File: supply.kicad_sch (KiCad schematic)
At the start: 71 parts, among them U1 AP7330-W5-7, U2 AP7330-W5-7, U3 AP7330-W5-7, U4 AP62301WU-7, U5 AP62301WU-7, U6 AP62301WU-7, U8 NCV51200MNTXG

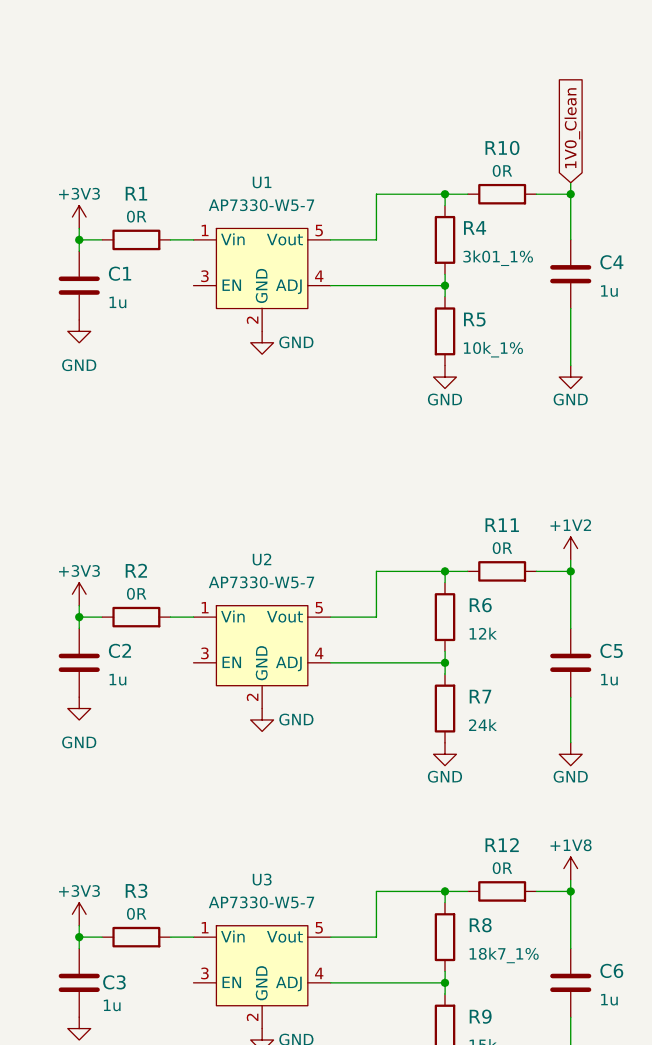
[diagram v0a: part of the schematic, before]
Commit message: Connected soft MIPI CSI to FPGA
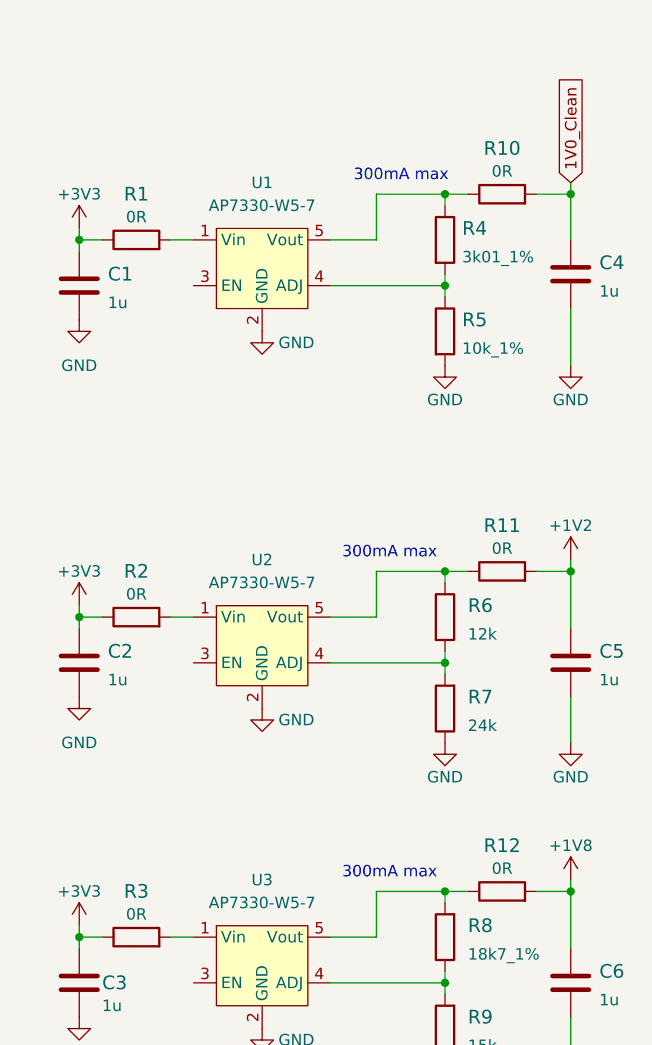
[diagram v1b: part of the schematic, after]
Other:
- note added: "300mA max"
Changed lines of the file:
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@@
     (stroke (width 0) (type default) (color 0 0 0 0))
+  )
+  (text "300mA max" (at 231.14 80.01 0)
+    (effects (font (size 1.27 1.27)) (justify left bottom))
   )
   (text "Sense line" (at 106.68 156.21 0)
@@
   )
   (text "Nominal currents are lower than rated" (at 115.57 138.43 0)
+    (effects (font (size 1.27 1.27)) (justify left bottom))
+  )
+  (text "300mA max" (at 231.14 115.57 0)
     (effects (font (size 1.27 1.27)) (justify left bottom))
   )
@@
     (effects (font (size 1.27 1.27)) (justify left bottom))
   )
+  (text "300mA max" (at 232.41 38.1 0)
+    (effects (font (size 1.27 1.27)) (justify left bottom))
+  )

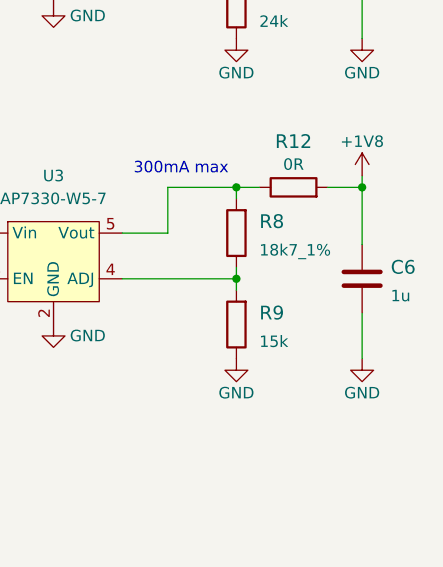
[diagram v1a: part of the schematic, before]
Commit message: Connected FPGA to power supply and added power filtering
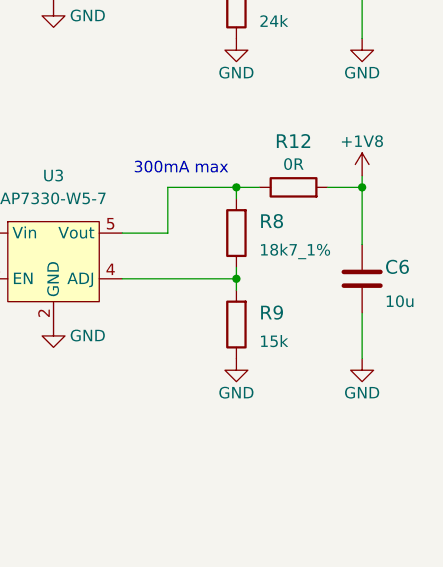
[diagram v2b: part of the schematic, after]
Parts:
- removed C6: C_1u_0603, antmicro-footprints:0603-cap, symbol antmicroCapacitors0603:C_1u_0603
- added C6: C_10u_0603, antmicro-footprints:0603-cap, symbol antmicroCapacitors0603:C_10u_0603
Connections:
- net +1V8: now also C6.1
- net GND: now also C6.2
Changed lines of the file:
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@@
-    (pin "2")
-  )
-  (symbol (lib_id "antmicroCapacitors0603:C_1u_0603") (at 256.54 127 0) (unit 1)
-    (in_bom yes) (on_board yes) (fields_autoplaced)
-    (property "Reference" "C6" (id 0) (at 259.715 125.73 0)
-      (effects (font (size 1.524 1.524)) (justify left))
-    )
-    (property "Value" "C_1u_0603" (id 1) (at 256.54 130.81 0)
-      (effects (font (size 1.524 1.524)) hide)
-    )
-    (property "Footprint" "antmicro-footprints:0603-cap" (id 2) (at 261.62 121.92 0)
-      (effects (font (size 1.524 1.524)) (justify left) hide)
-    )
-    (property "Datasheet" "" (id 3) (at 256.54 127 0)
-      (effects (font (size 1.27 1.27)) hide)
-    )
-    (property "Manufacturer" "WALSIN" (id 4) (at 261.62 116.84 0)
-      (effects (font (size 1.524 1.524)) (justify left) hide)
-    )
-    (property "MPN" "0603YD105KAT2A" (id 5) (at 261.62 119.38 0)
-      (effects (font (size 1.524 1.524)) (justify left) hide)
-    )
-    (property "Val" "1u" (id 6) (at 259.715 128.9049 0)
-      (effects (font (size 1.27 1.27)) (justify left))
-    )
-    (pin "1")
     (pin "2")
   )
@@
     (pin "1")
   )
+  (symbol (lib_id "antmicroCapacitors0603:C_10u_0603") (at 256.54 127 0) (unit 1)
+    (in_bom yes) (on_board yes)
+    (property "Reference" "C6" (id 0) (at 259.08 125.73 0)
+      (effects (font (size 1.524 1.524)) (justify left))
+    )
+    (property "Value" "C_10u_0603" (id 1) (at 256.54 130.81 0)
+      (effects (font (size 1.524 1.524)) hide)
+    )
+    (property "Footprint" "antmicro-footprints:0603-cap" (id 2) (at 261.62 121.92 0)
+      (effects (font (size 1.524 1.524)) (justify left) hide)
+    )
+    (property "Datasheet" "" (id 3) (at 256.54 127 0)
+      (effects (font (size 1.27 1.27)) hide)
+    )
+    (property "Manufacturer" "Murata" (id 4) (at 261.62 116.84 0)
+      (effects (font (size 1.524 1.524)) (justify left) hide)
+    )
+    (property "MPN" "GRM188R61A106KE69D" (id 5) (at 261.62 119.38 0)
+      (effects (font (size 1.524 1.524)) (justify left) hide)
+    )
+    (property "Val" "10u" (id 6) (at 259.08 129.54 0)
+      (effects (font (size 1.27 1.27)) (justify left))
+    )
+    (pin "1")
+    (pin "2")
+  )
   (symbol (lib_id "antmicroResistorsmisc:R_0R_0805") (at 160.02 24.765 0) (unit 1)

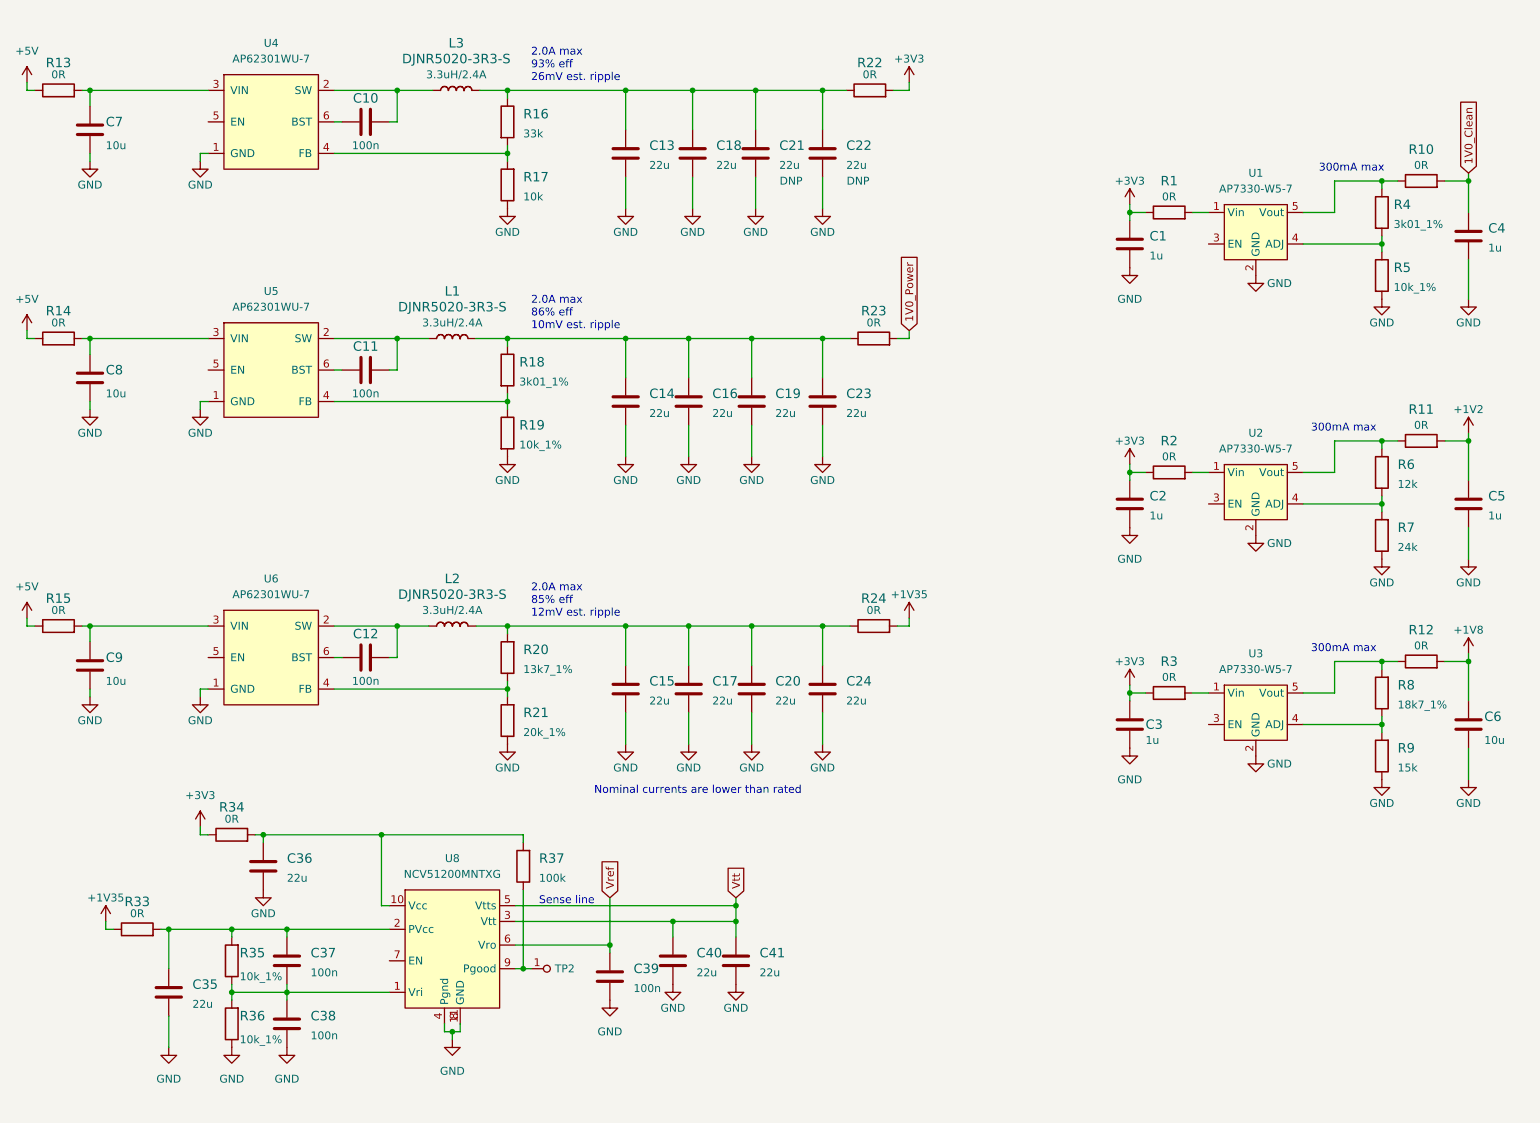
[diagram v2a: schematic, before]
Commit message: Connected EN pins on PSU schematic
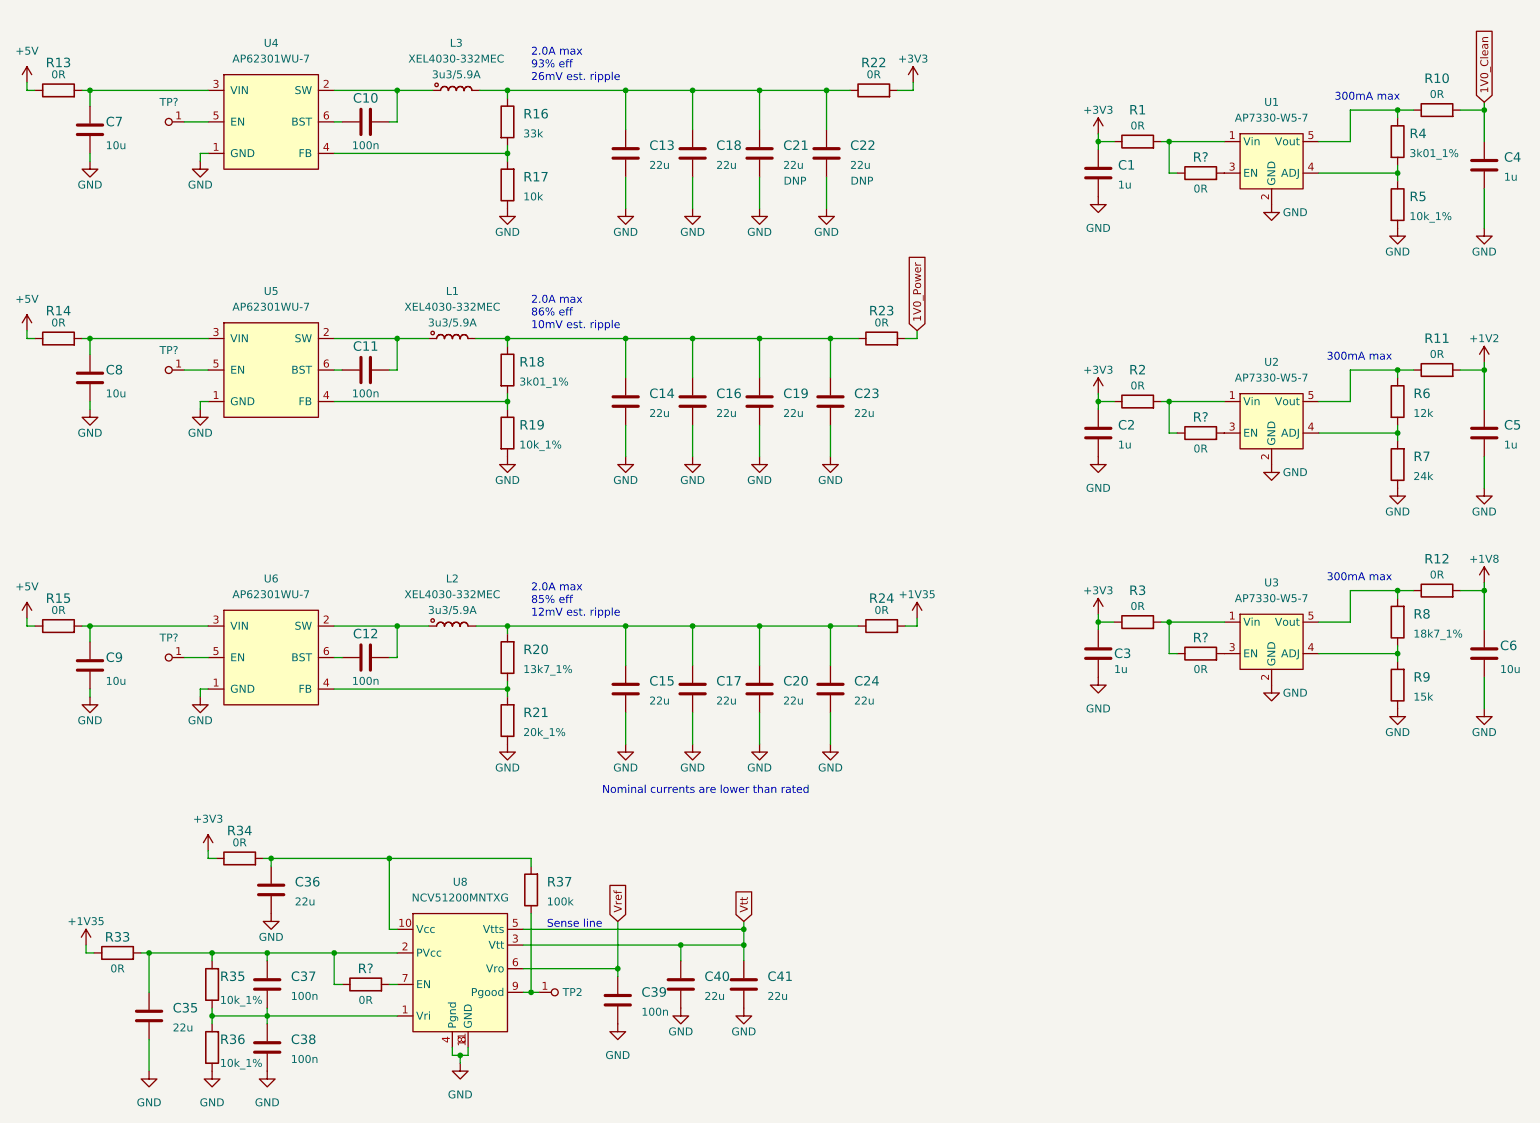
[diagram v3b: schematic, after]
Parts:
- removed L1, L2, L3: DJNR5020-3R3-S, crosslink-nx-video-converter:L_4.9x4.9mm, symbol crosslink-nx-video-converter:DJNR5020-3R3-S
- added L1, L2, L3: XEL4030-332MEC, antmicro-footprints:Coilcraft-XEL4030, symbol antmicroFixedInductors:XEL4030-332MEC
- added R? (x4): R_0R_0603, antmicro-footprints:0603-res, symbol antmicroResistors0603:R_0R_0603
- added TP? (x3): TP, antmicro-footprints:TP-R-1.5, symbol antmicroTestPoints:TP
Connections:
- net at C35.1, C37.1, R33.2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: now also R?.1
- net at U8.7 (EN): now also R?.2
- net at R1.2, U1.1 (Vin): now also R?.1
- net at U1.3 (EN): now also R?.2
- net at C14.1, C16.1, C19.1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: now also L1.2 (P)
- net at C12.2, U6.2 (SW): now also L2.1 (P)
- net at R2.2, U2.1 (Vin): now also R?.1
- net at C11.2, U5.2 (SW): now also L1.1 (P)
- net at C13.1, C18.1, C21.1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: now also L3.2 (P)
- net at C10.2, U4.2 (SW): now also L3.1 (P)
- net at C15.1, C17.1, C20.1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: now also L2.2 (P)
- net at R3.2, U3.1 (Vin): now also R?.1
- net at U2.3 (EN): now also R?.2
- net at U3.3 (EN): now also R?.2
- net at U4.5 (EN): now also TP?.1
- net at U6.5 (EN): now also TP?.1
- net at U5.5 (EN): now also TP?.1
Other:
- moved on the sheet: C1, C16, C17, C19, C2, C20, C21, C22, C23, C24, C3, C35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
